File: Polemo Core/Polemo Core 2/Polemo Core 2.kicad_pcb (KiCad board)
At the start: 4 copper layers, 40 x 100 mm, 174 parts, among them P1 Header-Male-2.54_2x2, P2 Header-Male-2.54_2x2, Q1 BC847_C2910145, Q2 MMBT5551LT1G, Q3 AO3401A, Q4 AO3401A, Q5 MMBT5551LT1G, U1 ATSAML21G18B-AUT, U10 74LVC1G08GV,125, U11 LT3014BHVES5#TRMPBF, U12 TXU0202DCUR, U13 TLV7031DBVR, U14 TLR341G-GTR, U15 803-87-006-10-001101, U2 XC6209F332MR-G, U3 MC14043BDR2G, U4 LMV793MFX/NOPB, U5 TPS7A2030PDBVR, U6 TLV3201AIDBVT, U7 OPA357AIDBVR, U8 TLR341G-GTR, U9 MF-ASML020/6-2, X1 32.768kHz

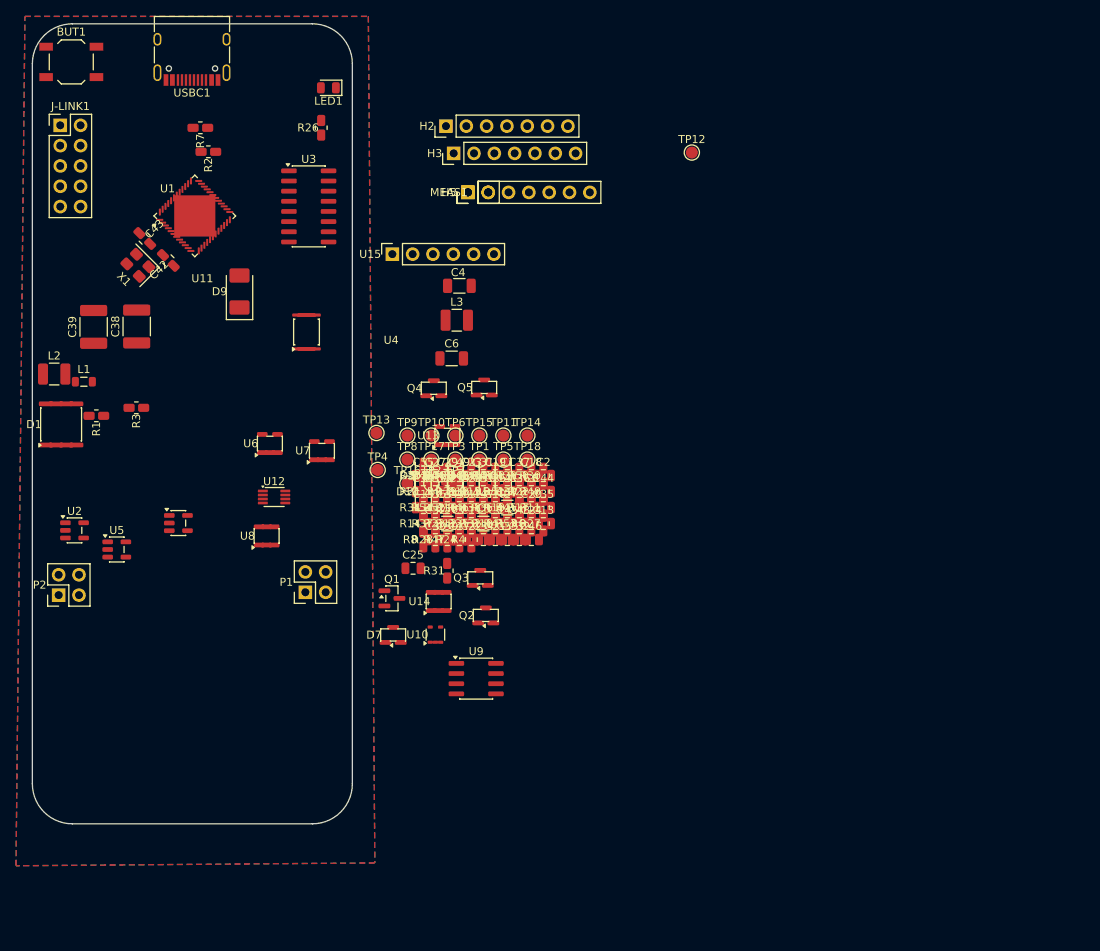
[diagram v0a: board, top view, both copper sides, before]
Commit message: Moved some components
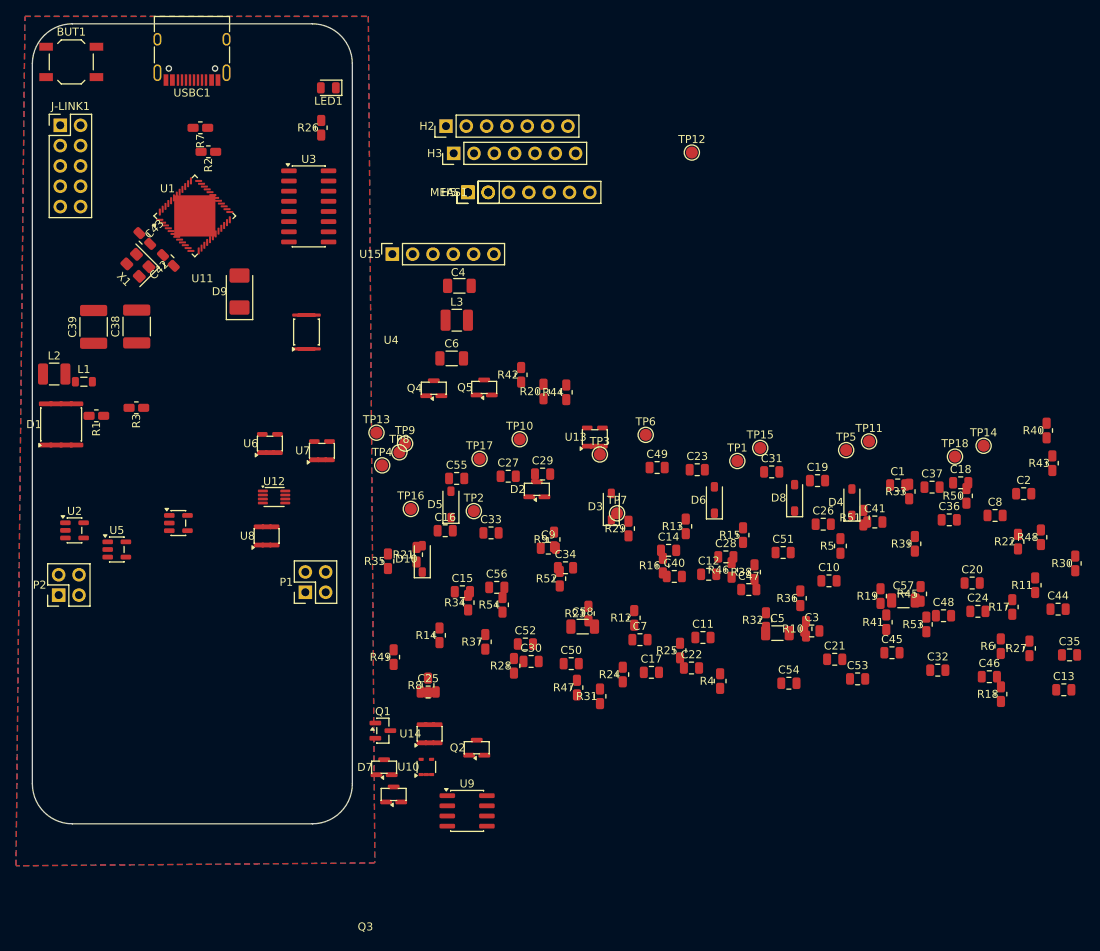
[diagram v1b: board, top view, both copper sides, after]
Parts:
- moved R40 70.6 mm to (176.8, 100.8)
- moved R43 69.6 mm to (177.5, 104.9)
- moved C35 68.3 mm to (179.6, 128.9)
- moved C13 68.3 mm to (178.9, 133.2)
- moved R18 67.5 mm to (171.1, 133.8)
- moved R30 67.4 mm to (180.4, 117.4)
- moved C44 66.0 mm to (178.2, 123.2)
- moved R27 62.7 mm to (174.6, 128.1)
- moved R48 62.5 mm to (176.1, 114.2)
- moved R11 62.2 mm to (175.4, 120.2)
- moved R17 61.4 mm to (172.5, 122.9)
- moved R22 61.1 mm to (173.2, 114.7)
- moved R6 60.6 mm to (171.1, 127.8)
- moved C2 60.1 mm to (173.9, 108.7)
- moved C46 59.8 mm to (169.6, 131.6)
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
